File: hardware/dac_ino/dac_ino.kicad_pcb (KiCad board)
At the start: 2 copper layers, 94 x 91 mm, 83 parts, among them J1 Conn_01x03_Male, J10 Conn_01x04, J11 Conn_01x02, J12 Molex 2 pin GATE IN, J13 Molex 2 pin GATE IN, J14 Conn_01x01_Units, J15 Molex 2 pin CV IN, J16 Molex 2 pin CV IN, J17 Molex 2 pin CV IN, J18 Molex 2 pin CV IN, J19 Molex 2 pin GATE IN, J2 Conn_01x03_Male, J20 Molex 2 pin GATE IN, J3 Molex 2 pin CV OUT, J4 Molex 2 pin CV OUT, J5 Molex 2 pin GATE OUT, J6 Molex 2 pin GATE OUT, J7 Conn_01x01_Units, J8 Molex 2 pin VCC, J9 EURO_PWR_2x5, Q1 2N3904, Q2 2N3904, Q3 2N3904, Q4 2N3904, Q5 2N3904, Q6 2N3904, U1 MCP4922, U2 TL072, U3 REF02CP+

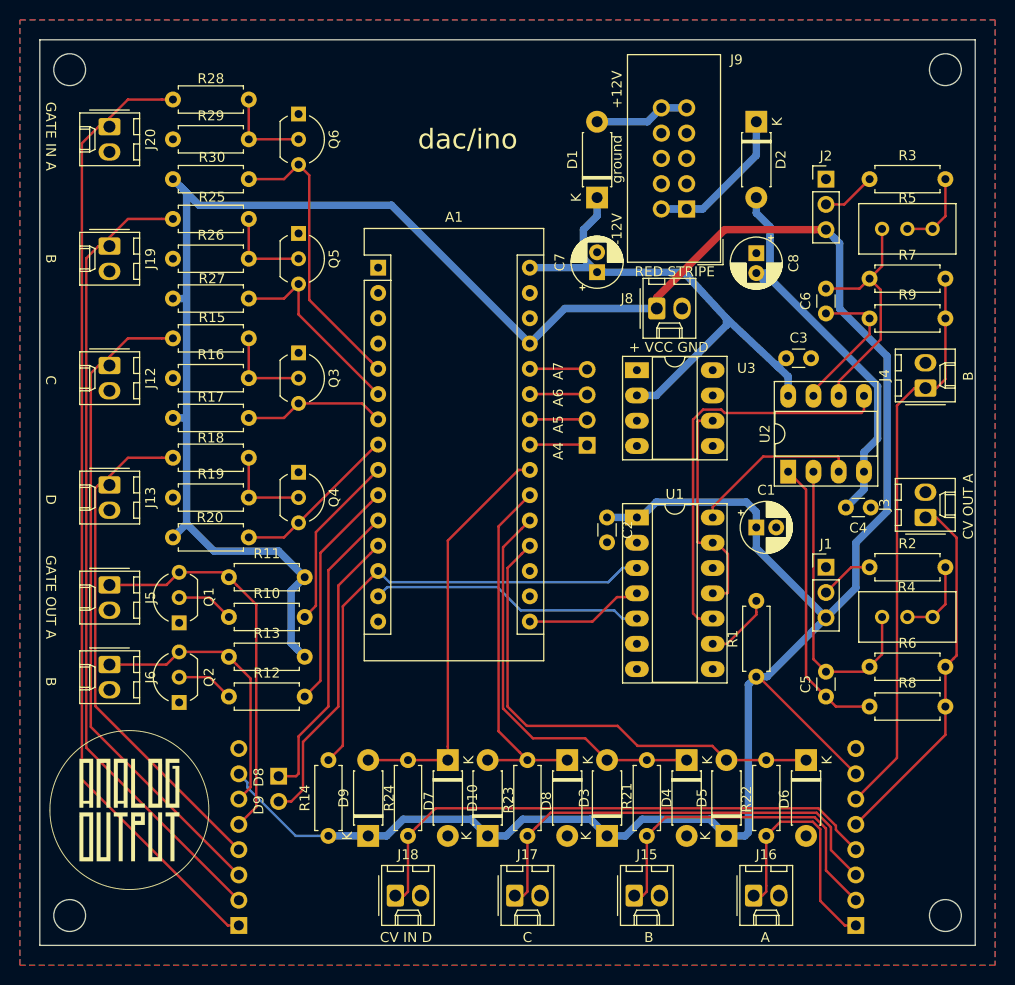
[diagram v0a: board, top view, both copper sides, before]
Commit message: Rearrange PCB to make headers easier to use
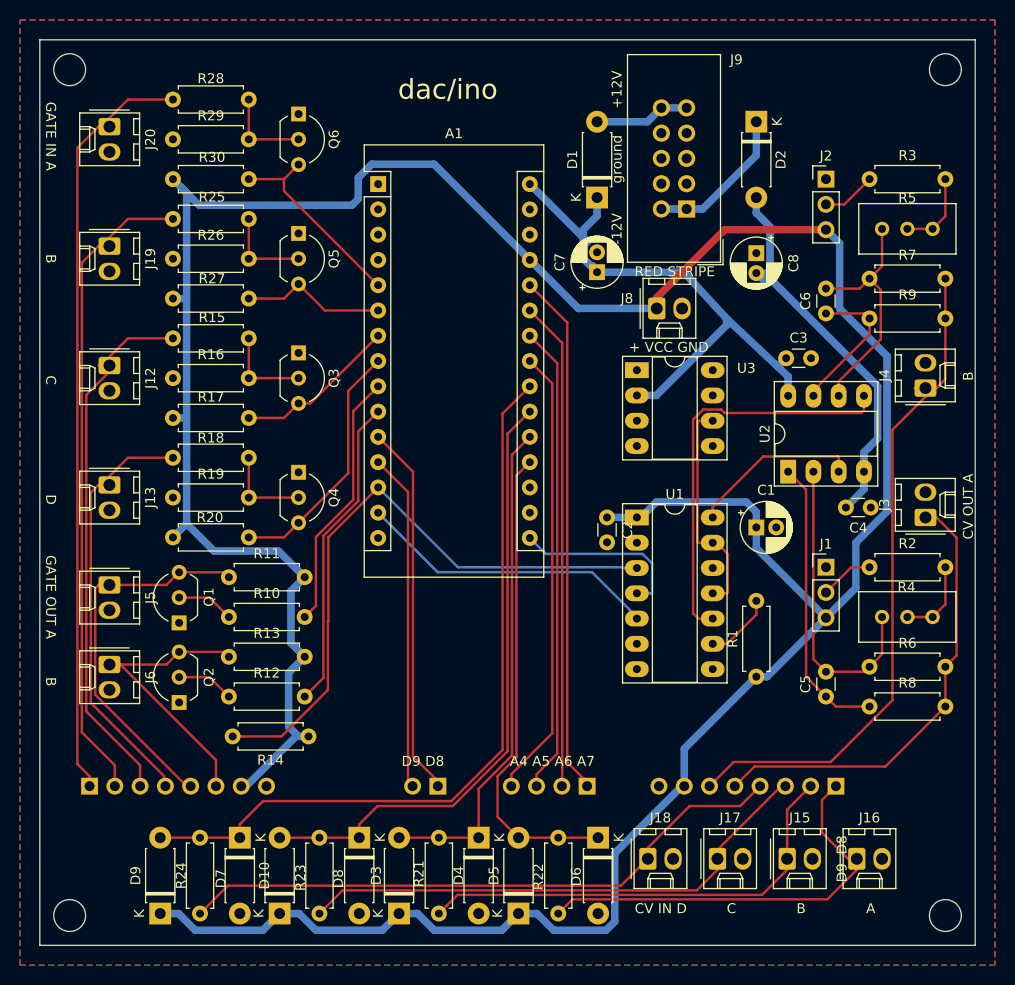
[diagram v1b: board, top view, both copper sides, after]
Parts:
- removed G***: LOGO, dac_ino:analogoutput2
- moved J10 34.2 mm to (195.0, 125.0), turned to 90 degrees
- moved J18 25.6 mm to (201.1, 132.3)
- moved D10 22.3 mm to (160.1, 130.2)
- moved D3 22.3 mm to (176.1, 137.8)
- moved D4 22.3 mm to (184.1, 130.2)
- moved D5 22.3 mm to (188.1, 137.8)
- moved D6 22.3 mm to (196.1, 130.2)
- moved D7 22.3 mm to (164.1, 137.8)
- moved D8 22.3 mm to (172.1, 130.2)
- moved D9 22.3 mm to (152.1, 137.8)
- moved R21 22.3 mm to (180.1, 130.2)
- moved R22 22.3 mm to (192.1, 130.2)
- moved R23 22.3 mm to (168.1, 130.2)
- moved R24 22.3 mm to (156.1, 130.2)
- moved J17 20.7 mm to (208.1, 132.3)
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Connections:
- J10 pad 1: /Arduino/A4 -> /Arduino/A7
- J10 pad 2: /Arduino/A5 -> /Arduino/A6
- J10 pad 3: /Arduino/A6 -> /Arduino/A5
- J10 pad 4: /Arduino/A7 -> /Arduino/A4
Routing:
- net /Arduino/A7: track 5.79 -> 51.8 mm
- net /Arduino/A6: track 5.85 -> 49.2 mm
- net /Arduino/A5: track 5.79 -> 47.3 mm
- net /Arduino/A4: track 5.79 -> 45.4 mm
- net /Arduino/A3: track 41.2 -> 76.5 mm
- net /Arduino/A2: track 37.1 -> 62.4 mm
- net /Inputs/Gate in A/GATE_IN: track 97.3 -> 76.8 mm
- net /Inputs/CV in A/CV_IN: track 25.2 -> 42.8 mm
- net /Inputs/Gate in B/GATE_IN: track 81.7 -> 65.5 mm
- net /Arduino/DAC_CS: track 48.1 -> 63.3 mm
- net VCC: track 310.9 -> 323.9 mm
- net /Inputs/Gate in C/GATE_IN: track 66.8 -> 54.6 mm
- net /Inputs/CV in B/CV_IN: track 34.7 -> 46.2 mm
- net /CV out/CV_OUT_B: track 57.3 -> 68.3 mm
- net /Arduino/A1: track 40.6 -> 50.4 mm
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
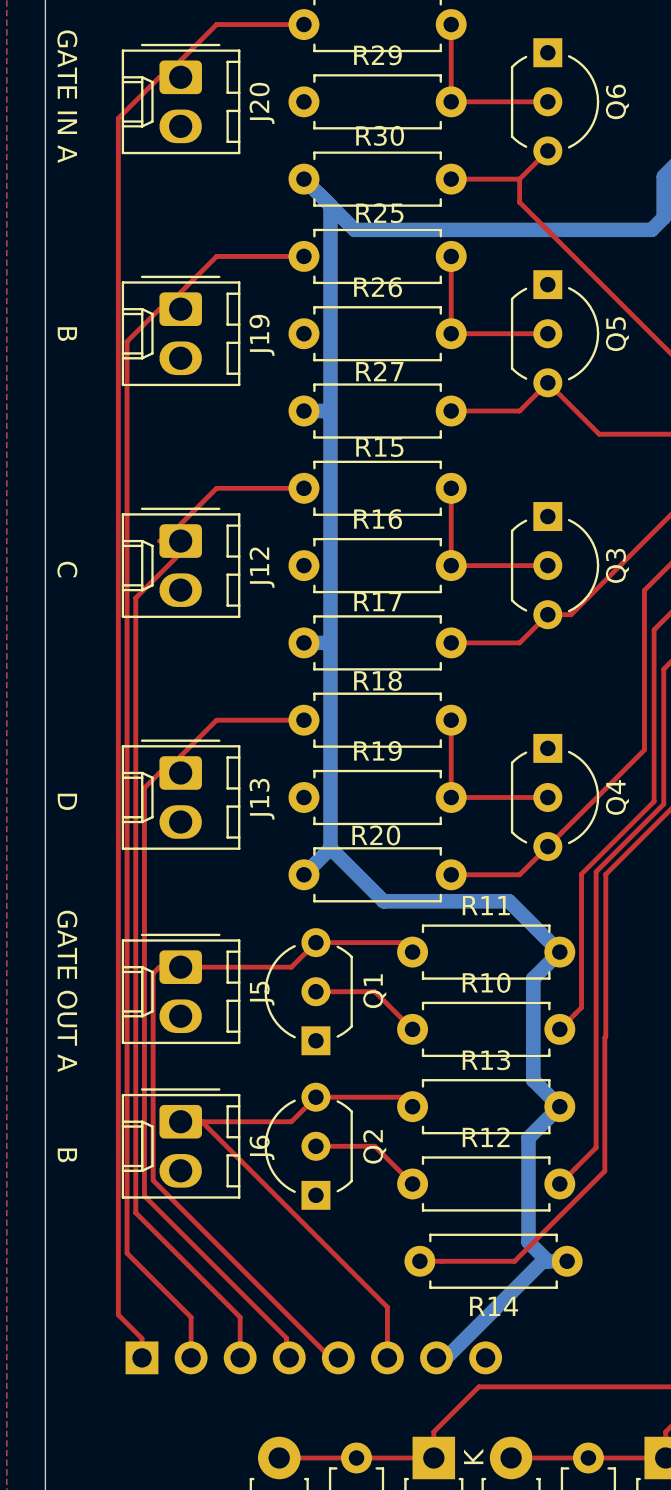
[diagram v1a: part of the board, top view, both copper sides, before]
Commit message: Reorient header
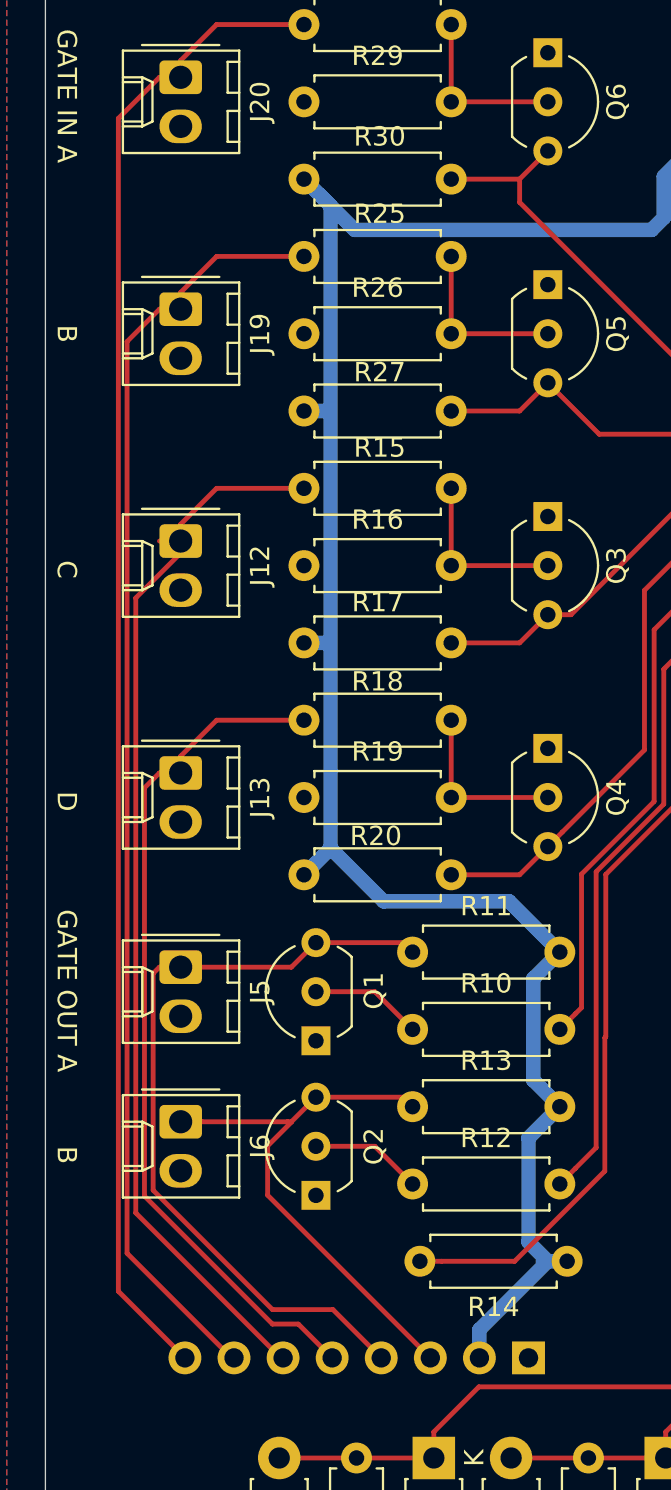
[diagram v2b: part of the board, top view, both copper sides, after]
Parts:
- moved J7 20.0 mm to (165.0, 125.0), turned to 90 degrees
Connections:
- J7 pad 1: /Inputs/Gate in A/GATE_IN -> GND
- J7 pad 2: /Inputs/Gate in B/GATE_IN -> VCC
- J7 pad 3: /Inputs/Gate in C/GATE_IN -> /Gate out/GATE_OUT_B
- J7 pad 4: /Inputs/Gate in D/GATE_IN -> /Gate out/GATE_OUT_A
- J7 pad 5: /Gate out/GATE_OUT_A -> /Inputs/Gate in D/GATE_IN
- J7 pad 6: /Gate out/GATE_OUT_B -> /Inputs/Gate in C/GATE_IN
- J7 pad 7: VCC -> /Inputs/Gate in B/GATE_IN
- J7 pad 8: GND -> /Inputs/Gate in A/GATE_IN
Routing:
- net /Gate out/GATE_OUT_A: track 38.4 -> 40.9 mm
- net /Inputs/Gate in D/GATE_IN: track 42.8 -> 44.9 mm
- net /Inputs/Gate in C/GATE_IN: track 54.6 -> 55.8 mm
- net VCC: track 323.9 -> 322.8 mm
- net /Inputs/Gate in B/GATE_IN: track 65.5 -> 66.4 mm
- net /Inputs/Gate in A/GATE_IN: track 76.8 -> 77.7 mm

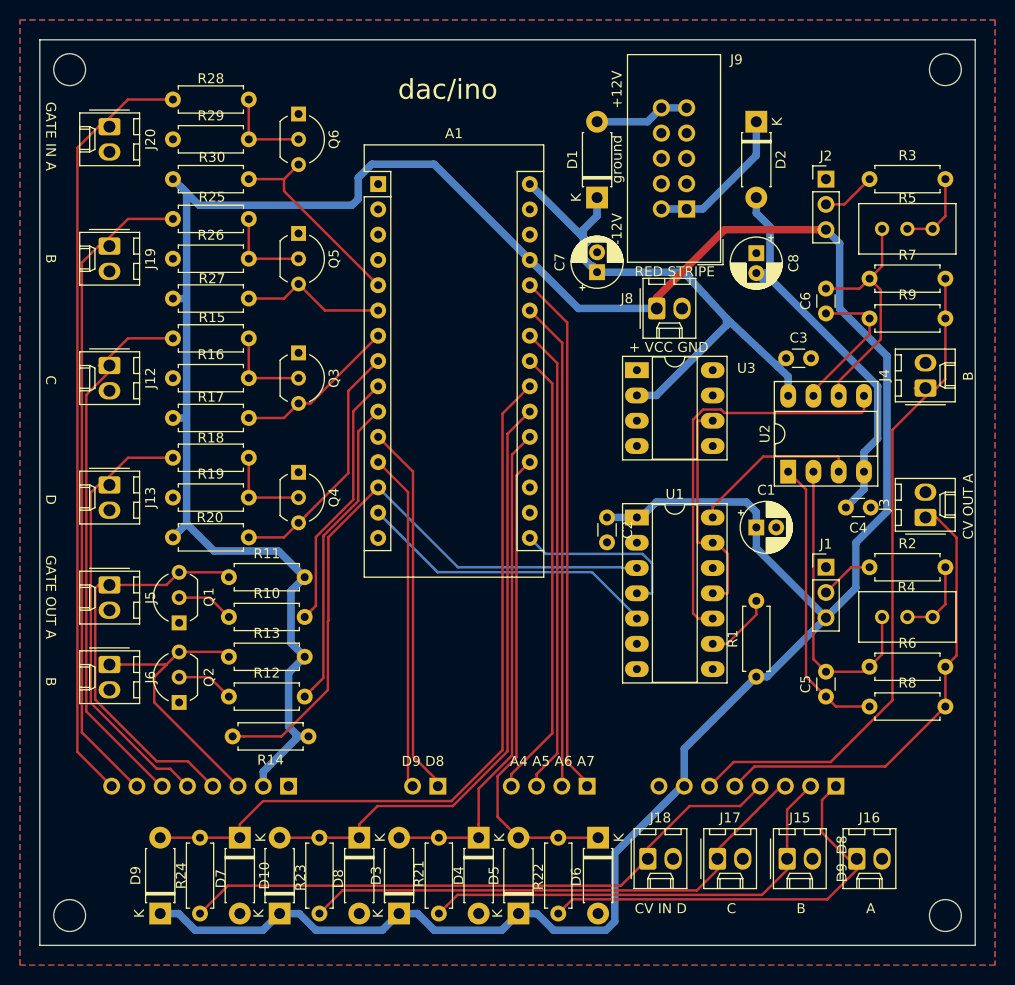
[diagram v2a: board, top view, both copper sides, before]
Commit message: Rearrange 8 pin Molex; convert footprints to AO versions and clean up silkscreen
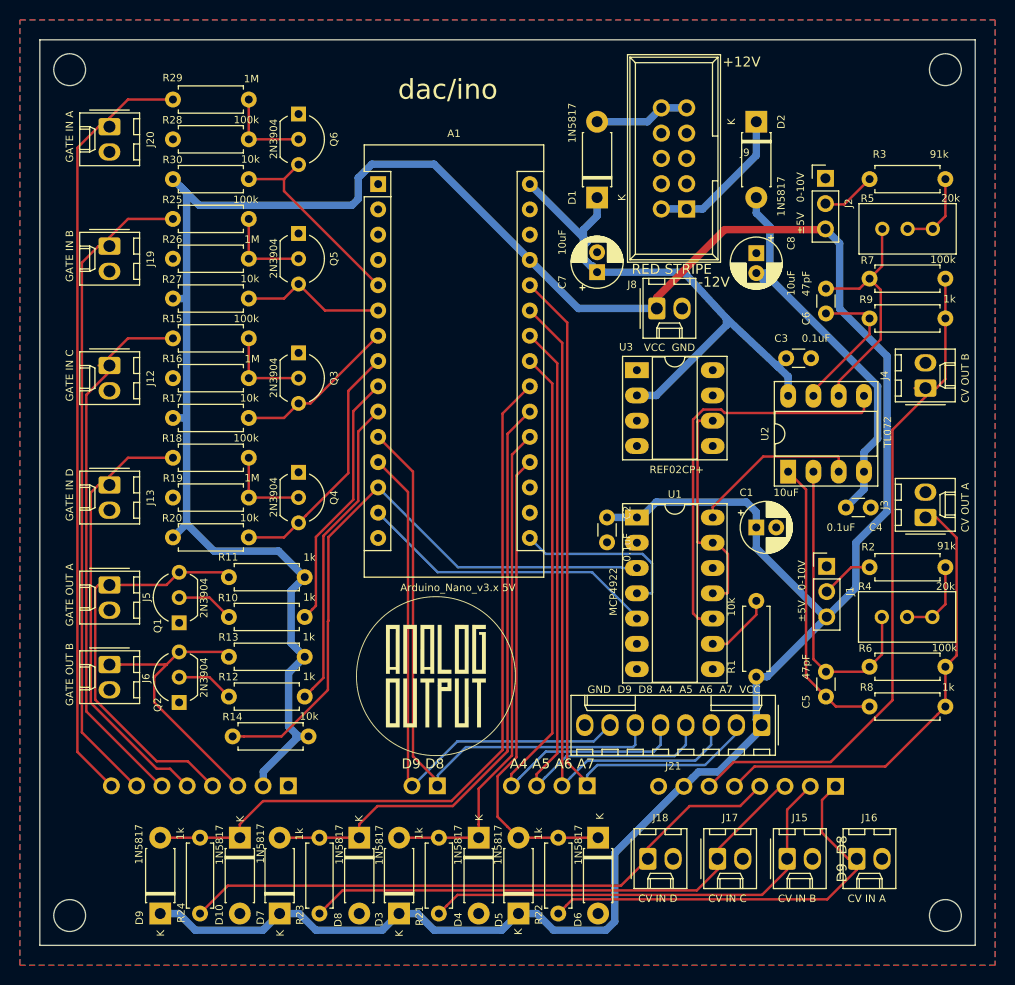
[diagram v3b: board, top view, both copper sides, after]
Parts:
- added G***: LOGO, ao_tht:analogoutput, F.Cu at (179.8, 113.9)
- added J21: Conn_01x06, ao_tht:Molex_KK-254_AE-6410-08A_1x08_P2.54mm_Vertical, F.Cu at (212.5, 118.9)
- A1: footprint Module:Arduino_Nano -> ao_tht:Arduino_Nano
- C1, C7, C8: footprint Capacitor_THT:CP_Radial_D5.0mm_P2.00mm -> ao_tht:CP_Radial_D5.0mm_P2.00mm
- C2, C3, C4, C5, C6: footprint Capacitor_THT:C_Disc_D3.0mm_W1.6mm_P2.50mm -> ao_tht:C_Disc_D3.0mm_W1.6mm_P2.50mm
- D1, D10, D2, D3, D4, D5, D6, D7, D8, D9: footprint Diode_THT:D_DO-41_SOD81_P7.62mm_Horizontal -> ao_tht:D_DO-41_SOD81_P7.62mm_Horizontal
- H1, H2, H3, H4: footprint MountingHole:MountingHole_3.2mm_M3 -> ao_tht:MountingHole_3.2mm_M3
- J1, J2: footprint Connector_PinHeader_2.54mm:PinHeader_1x03_P2.54mm_Vertical -> ao_tht:PinHeader_1x03_P2.54mm_Vertical
- J10: footprint Connector_PinHeader_2.54mm:PinHeader_1x04_P2.54mm_Vertical -> ao_tht:PinHeader_1x04_P2.54mm_Vertical
- J11: footprint Connector_PinHeader_2.54mm:PinHeader_1x02_P2.54mm_Vertical -> ao_tht:PinHeader_1x02_P2.54mm_Vertical
- J12, J13, J15, J16, J17, J18, J19, J20, J3, J4, J5, J6, J8: footprint Connector_Molex:Molex_KK-254_AE-6410-02A_1x02_P2.54mm_Vertical -> ao_tht:Molex_KK-254_AE-6410-02A_1x02_P2.54mm_Vertical
- J14, J7: footprint Connector_PinHeader_2.54mm:PinHeader_1x08_P2.54mm_Vertical -> ao_tht:PinHeader_1x08_P2.54mm_Vertical
- J9: footprint Connector_IDC:IDC-Header_2x05_P2.54mm_Vertical -> ao_tht:Power_Header
- Q1, Q2, Q3, Q4, Q5, Q6: footprint Package_TO_SOT_THT:TO-92_Inline_Wide -> ao_tht:TO-92_Inline_Wide
- R1, R10, R11, R12, R13, R14, R15, R16, R17, R18, R19, R2, R20, R21, R22, R23, R24, R25, R26, R27, R28, R29, R3, R30, R6, R7, R8, R9: footprint Resistor_THT:R_Axial_DIN0207_L6.3mm_D2.5mm_P7.62mm_Horizontal -> ao_tht:R_Axial_DIN0207_L6.3mm_D2.5mm_P7.62mm_Horizontal
- R4, R5: footprint Potentiometer_THT:Potentiometer_Bourns_3296W_Vertical -> ao_tht:Potentiometer_Bourns_3296W_Vertical
- U1: footprint Package_DIP:DIP-14_W7.62mm_Socket_LongPads -> ao_tht:DIP-14_W7.62mm_Socket_LongPads
- U2, U3: footprint Package_DIP:DIP-8_W7.62mm_Socket_LongPads -> ao_tht:DIP-8_W7.62mm_Socket_LongPads
- moved J14 8.93 mm to (211.1, 124.9), turned to 180 degrees
- moved J7 8.92 mm to (156.1, 124.8), turned to 180 degrees
- moved J10 3.88 mm to (191.1, 124.7), turned to 180 degrees
- moved R5 2.56 mm to (227.2, 69.0)
- moved R4 2.51 mm to (227.2, 108.0)
- moved J2 2.42 mm to (218.9, 66.4), turned to 270 degrees
- moved J1 2.41 mm to (219.1, 105.4), turned to 270 degrees
- moved J11 1.06 mm to (178.9, 125.0), turned to 180 degrees
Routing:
- net /Arduino/D8: track 37.6 -> 61.8 mm
- net /Arduino/D9: track 34.0 -> 56.4 mm
- net /Arduino/A6: track 49.2 -> 67.9 mm
- net /Arduino/A5: track 47.3 -> 66.0 mm
- net /Arduino/A4: track 45.4 -> 64.1 mm
- net /Arduino/A7: track 51.8 -> 70.5 mm
- net VCC: track 322.8 -> 324.4 mm
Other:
- board text added: "dac/ino • Rich Holmes 7/2020 • from Synapse by Vincenzo Pacella • cc-by-ca"
- board text removed: "+ VCC GND"
- board text removed: "+12V"
- board text removed: "-12V"
- board text removed: "A"
- board text removed: "B"
- board text removed: "C"
- board text removed: "CV IN D"
- board text removed: "CV OUT A"
- board text removed: "D"
- board text removed: "GATE IN A"
- board text removed: "GATE OUT A"
- board text removed: "RED STRIPE"
- board text removed: "dac/ino • Rich Holmes 5/2020 • from Synapse by Vincenzo Pacella • cc-by-ca"
- board text removed: "ground"
